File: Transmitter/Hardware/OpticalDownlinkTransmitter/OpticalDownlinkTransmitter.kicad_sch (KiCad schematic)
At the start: 34 parts, among them J1 Conn_01x04_Pin, J2 Conn_01x04_Pin, U1 AL8860MP, U2 AL8860MP, U3 AL8860MP, U4 AL8860MP

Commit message: Assigned a couple footprints
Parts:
- D11, D12, D13, D14, D15, D16, D7, D8: footprint (none) -> Footprint Library:OD624L
- D3, D4, D5, D6: footprint SamacSys_Parts:OD624L -> Footprint Library:OD624L
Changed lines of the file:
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@@
 			)
 		)
-		(property "Footprint" ""
+		(property "Footprint" "Footprint Library:OD624L"
 			(at 252.73 57.15 0)
 			(effects
@@
 			)
 		)
-		(property "Footprint" "SamacSys_Parts:OD624L"
+		(property "Footprint" "Footprint Library:OD624L"
 			(at 149.86 67.31 0)
 			(effects
@@
 			)
 		)
-		(property "Footprint" ""
+		(property "Footprint" "Footprint Library:OD624L"
 			(at 149.86 133.35 0)
 			(effects
@@
 			)
 		)
-		(property "Footprint" ""
+		(property "Footprint" "Footprint Library:OD624L"
 			(at 252.73 143.51 0)
 			(effects
@@
 			)
 		)
-		(property "Footprint" ""
+		(property "Footprint" "Footprint Library:OD624L"
 			(at 252.73 67.31 0)
 			(effects
@@
 			)
 		)
-		(property "Footprint" "SamacSys_Parts:OD624L"
+		(property "Footprint" "Footprint Library:OD624L"
 			(at 144.78 52.07 0)
 			(effects
@@
 			)
 		)
-		(property "Footprint" ""
+		(property "Footprint" "Footprint Library:OD624L"
 			(at 247.65 128.27 0)
 			(effects
@@
 			)
 		)
-		(property "Footprint" ""
+		(property "Footprint" "Footprint Library:OD624L"
 			(at 149.86 143.51 0)
 			(effects
@@
 			)
 		)
-		(property "Footprint" "SamacSys_Parts:OD624L"
+		(property "Footprint" "Footprint Library:OD624L"
 			(at 144.78 128.27 0)
 			(effects
@@
 			)
 		)
-		(property "Footprint" ""
+		(property "Footprint" "Footprint Library:OD624L"
 			(at 247.65 52.07 0)
 			(effects
@@
 			)
 		)
-		(property "Footprint" ""
+		(property "Footprint" "Footprint Library:OD624L"
 			(at 252.73 133.35 0)
 			(effects
@@
 			)
 		)
-		(property "Footprint" "SamacSys_Parts:OD624L"
+		(property "Footprint" "Footprint Library:OD624L"
 			(at 149.86 57.15 0)
 			(effects

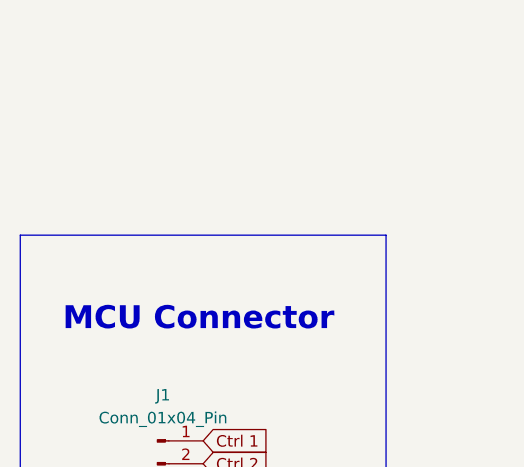
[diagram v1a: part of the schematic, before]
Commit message: Assigned a couple footprints and started adding JLBPCB Parts
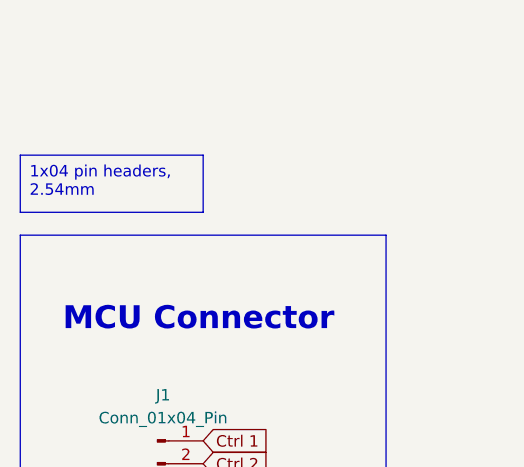
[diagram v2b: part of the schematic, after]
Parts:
- D3, D5, D6: JLCPCB Part (none) -> C20010764
- R1: footprint (none) -> Resistor_SMD:R_0805_2012Metric_Pad1.20x1.40mm_HandSolder; JLBPCB Part (none) -> C20485079
- R2: footprint (none) -> Resistor_SMD:R_0805_2012Metric_Pad1.20x1.40mm_HandSolder; Digikey Part (none) -> RLC73K2AR287FTD; JLCPCB Part (none) -> C20485079
- R3, R4: footprint (none) -> Resistor_SMD:R_0805_2012Metric_Pad1.20x1.40mm_HandSolder; JLCPCB Part (none) -> C20485079
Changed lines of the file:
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@@
 		)
 	)
+	(text_box "1x04 pin headers, 2.54mm\n"
+		(exclude_from_sim no)
+		(at 22.86 41.91 0)
+		(size 20.32 6.35)
+		(stroke
+			(width 0)
+			(type default)
+		)
+		(fill
+			(type none)
+		)
+		(effects
+			(font
+				(size 1.27 1.27)
+			)
+			(justify left top)
+		)
+	)
 	(text_box "I_{f} of each LED = 350mA\n\nR = 0.1/i_{out_nom} = 0.1/0.35A = 0.285  (p.11)"
 		(exclude_from_sim no)
@@
 			)
 		)
-		(property "Footprint" ""
+		(property "Footprint" "Resistor_SMD:R_0805_2012Metric_Pad1.20x1.40mm_HandSolder"
 			(at 236.22 126.492 90)
 			(effects
@@
 			)
 		)
+		(property "JLCPCB Part" "C20485079"
+			(at 236.22 128.27 90)
+			(effects
+				(font
+					(size 1.27 1.27)
+				)
+				(hide yes)
+			)
+		)
 		(pin "2"
 		)
@@
 			)
 		)
-		(property "Footprint" ""
+		(property "Footprint" "Resistor_SMD:R_0805_2012Metric_Pad1.20x1.40mm_HandSolder"
 			(at 133.35 50.292 90)
 			(effects
@@
 			)
 		)
+		(property "JLBPCB Part" "C20485079"
+			(at 133.35 52.07 90)
+			(effects
+				(font
+					(size 1.27 1.27)
+				)
+				(hide yes)
+			)
+		)
 		(pin "2"
 		)
@@
 			)
 		)
+		(property "JLCPCB Part" "C20010764"
+			(at 149.86 67.31 0)
+			(effects
+				(font
+					(size 1.27 1.27)
+				)
+				(hide yes)
+			)
+		)
 		(pin "1"
 		)
@@
 			)
 		)
+		(property "JLCPCB Part" "C20010764"
+			(at 144.78 52.07 0)
+			(effects
+				(font
+					(size 1.27 1.27)
+				)
+				(hide yes)
+			)
+		)
 		(pin "2"
 		)
@@
 			)
 		)
-		(property "Footprint" ""
+		(property "Footprint" "Resistor_SMD:R_0805_2012Metric_Pad1.20x1.40mm_HandSolder"
 			(at 236.22 50.292 90)
 			(effects
@@
 			)
 		)
+		(property "JLCPCB Part" "C20485079"
+			(at 236.22 52.07 90)
+			(effects
+				(font
+					(size 1.27 1.27)
+				)
+				(hide yes)
+			)
+		)
 		(pin "2"
 		)
@@
 			)
 		)
-		(property "Footprint" ""
+		(property "Footprint" "Resistor_SMD:R_0805_2012Metric_Pad1.20x1.40mm_HandSolder"
 			(at 133.35 126.492 90)
 			(effects
@@
 			)
 		)
+		(property "Digikey Part" "RLC73K2AR287FTD"
+			(at 133.35 128.27 90)
+			(effects
+				(font
+					(size 1.27 1.27)
+				)
+				(hide yes)
+			)
+		)
+		(property "JLCPCB Part" "C20485079"
+			(at 133.35 128.27 90)
+			(effects
+				(font
+					(size 1.27 1.27)
+				)
+				(hide yes)
+			)
+		)
 		(pin "2"
 		)
@@
 			(at 149.86 57.15 0)
 			(effects
+				(font
+					(size 1.27 1.27)
+				)
+				(hide yes)
+			)
+		)
+		(property "JLCPCB Part" "C20010764"
+			(at 149.86 57.15 0)
+			(effects

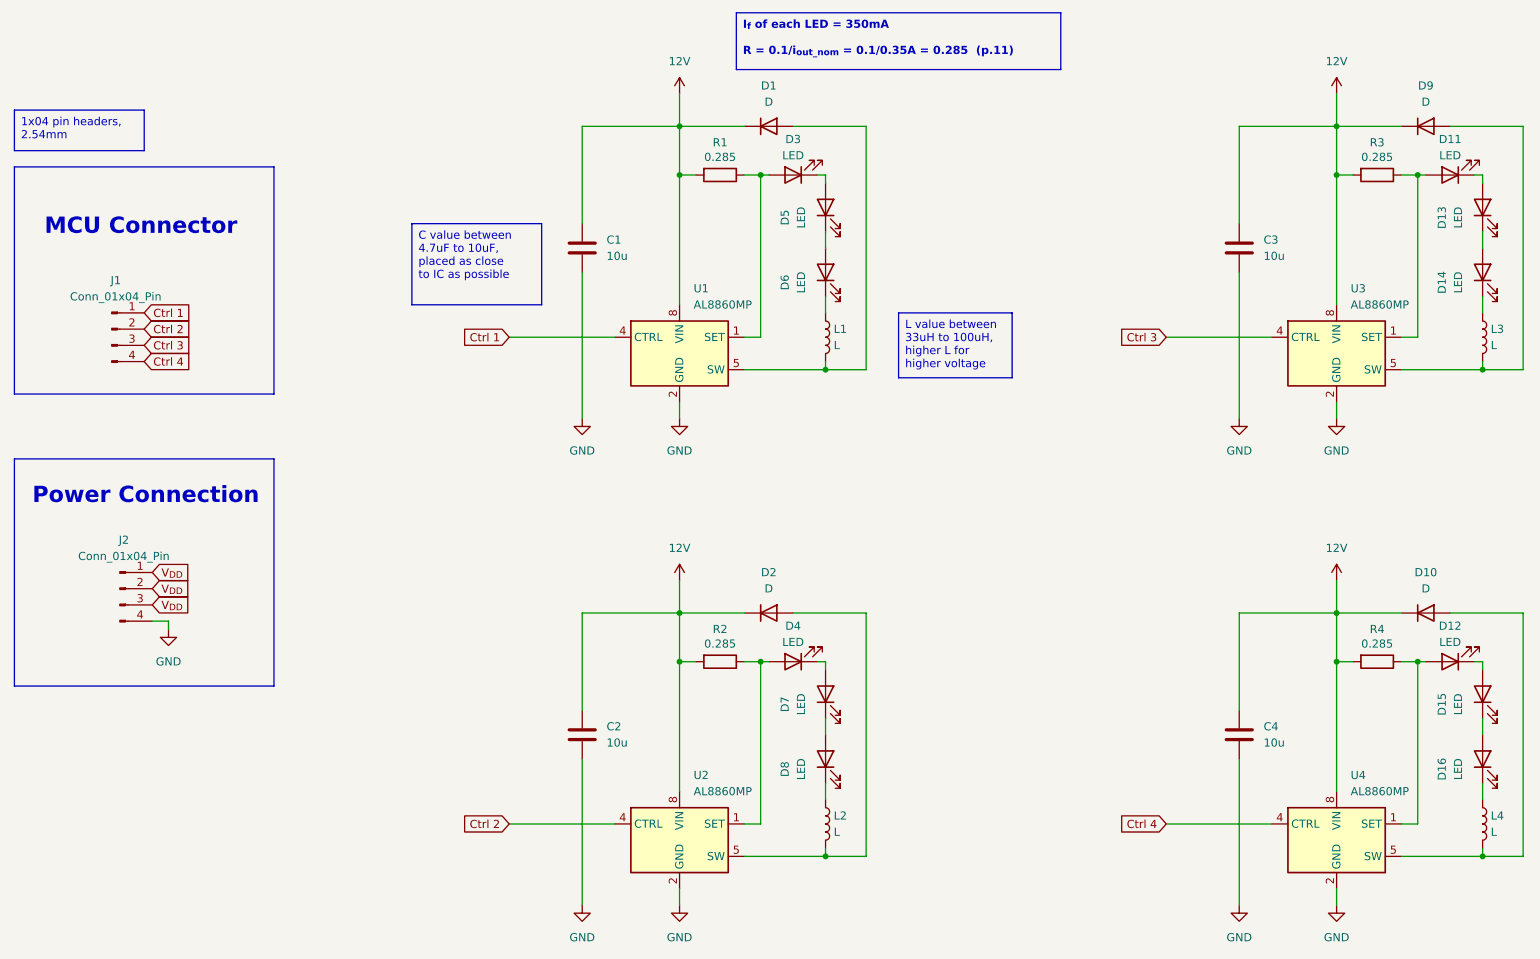
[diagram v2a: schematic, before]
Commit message: Assigned JLCPCB Parts and footprints
Inductor is the remaining component left to find
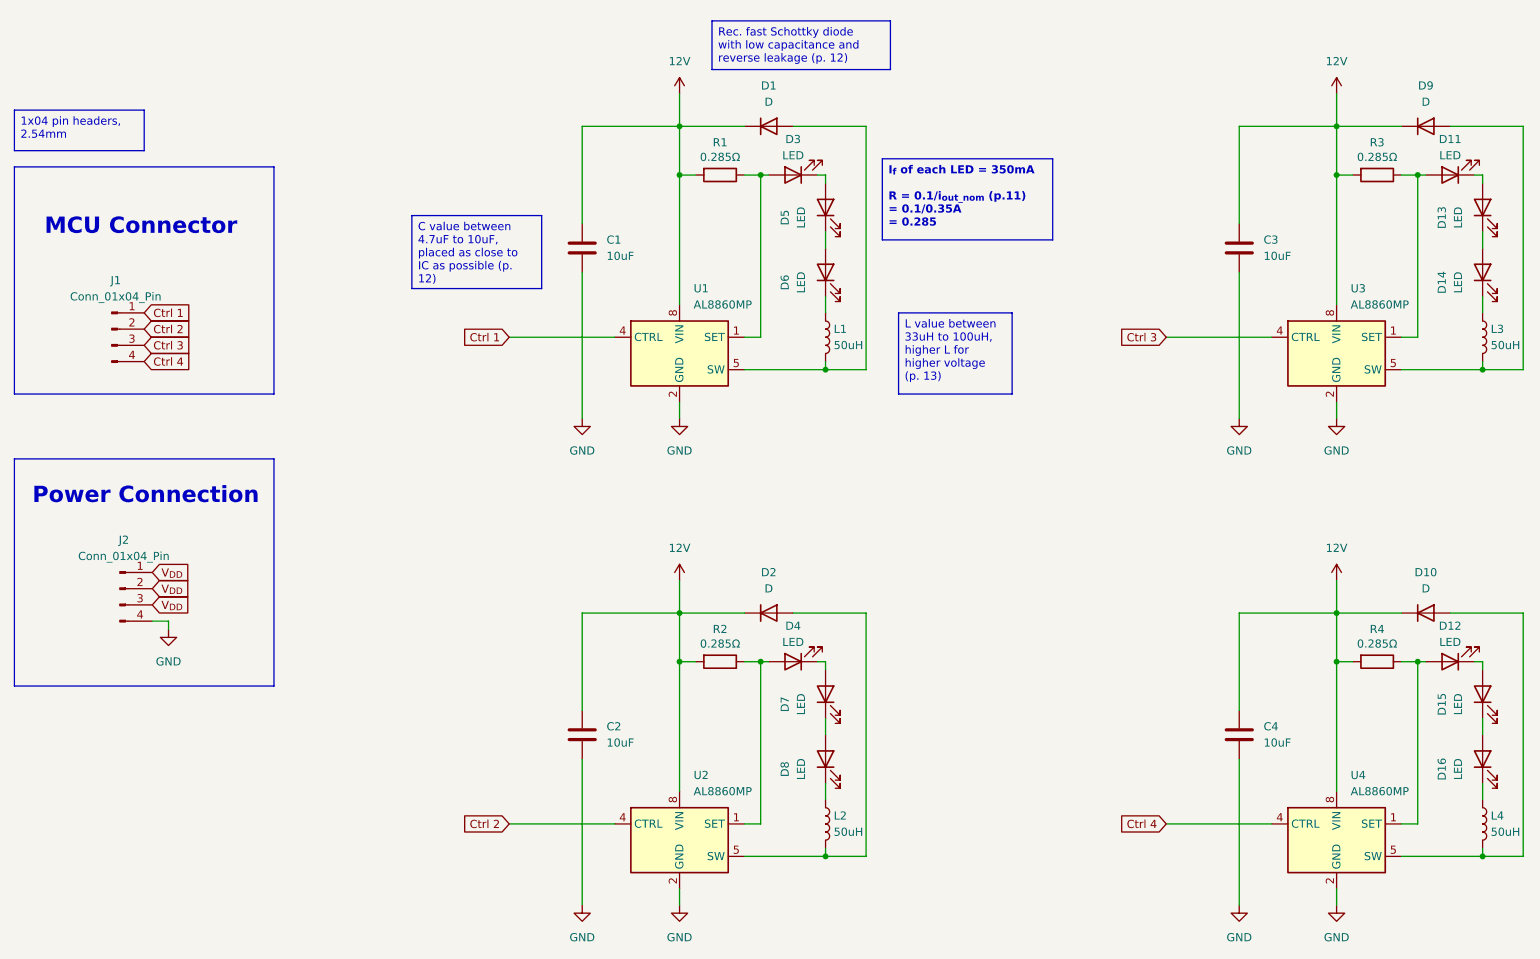
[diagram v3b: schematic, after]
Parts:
- C1, C2, C3, C4: value 10u -> 10uF
- D1, D10, D2, D9: footprint (none) -> Footprint Library:P2_DO-201; JLCPCB Part (none) -> C5357977
- D11, D12, D13, D14, D15, D16, D4, D7, D8: JLCPCB Part (none) -> C20010764
- J1, J2: footprint (none) -> Connector_PinSocket_2.54mm:PinSocket_1x04_P2.54mm_Vertical
- L1, L2, L3, L4: value L -> 50uH
- R1, R2, R3, R4: value 0.285 -> 0.285Ω
- U1, U2, U3, U4: JLCPCB Part (none) -> C500782

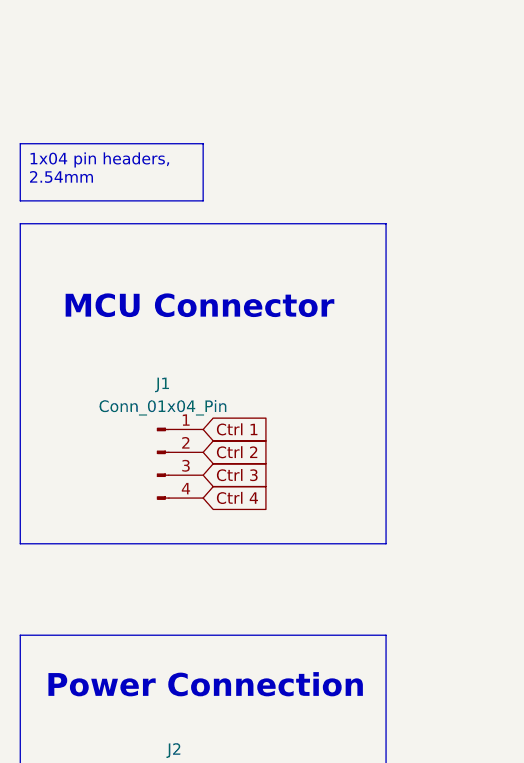
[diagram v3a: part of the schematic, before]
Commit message: Assigned JLCPCB Parts
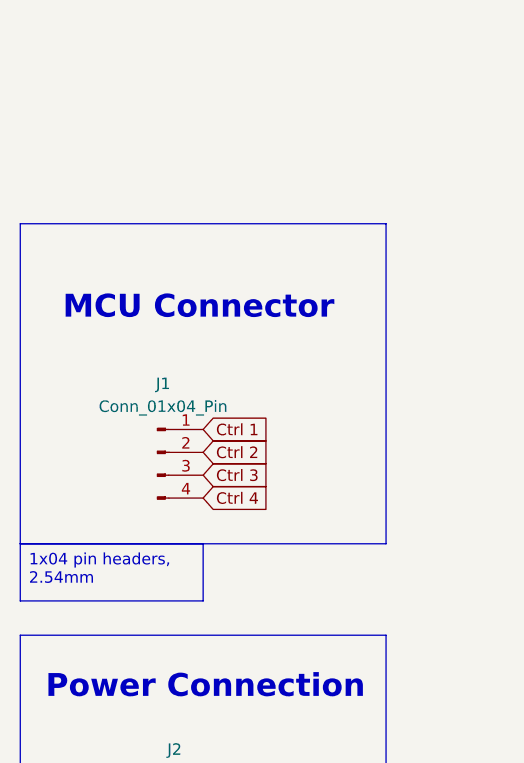
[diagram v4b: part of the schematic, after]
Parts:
- C1, C2, C3, C4: footprint (none) -> Capacitor_SMD:C_0805_2012Metric_Pad1.18x1.45mm_HandSolder; JLCPCB Part (none) -> C95841
- L1, L2, L3, L4: footprint (none) -> Footprint Library:DR125; JLCPCB Part (none) -> C5120951
- R1: JLBPCB Part C20485079 -> (none); JLCPCB Part (none) -> C20485079
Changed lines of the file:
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@@
 	(text_box "1x04 pin headers, 2.54mm\n"
 		(exclude_from_sim no)
-		(at 22.86 41.91 0)
+		(at 22.86 86.36 0)
 		(size 20.32 6.35)
 		(margins 0.9525 0.9525 0.9525 0.9525)
@@
 			)
 		)
-		(property "Footprint" ""
+		(property "Footprint" "Footprint Library:DR125"
 			(at 252.73 77.47 0)
 			(effects
@@
 			)
 		)
+		(property "JLCPCB Part" "C5120951"
+			(at 252.73 77.47 0)
+			(effects
+				(font
+					(size 1.27 1.27)
+				)
+				(hide yes)
+			)
+		)
 		(pin "1"
 		)
@@
 			)
 		)
-		(property "Footprint" ""
+		(property "Footprint" "Footprint Library:DR125"
 			(at 149.86 77.47 0)
 			(effects
@@
 			)
 		)
+		(property "JLCPCB Part" "C5120951"
+			(at 149.86 77.47 0)
+			(effects
+				(font
+					(size 1.27 1.27)
+				)
+				(hide yes)
+			)
+		)
 		(pin "1"
 		)
@@
 			)
 		)
-		(property "JLBPCB Part" "C20485079"
+		(property "JLCPCB Part" "C20485079"
 			(at 133.35 52.07 90)
 			(effects
@@
 			)
 		)
-		(property "Footprint" ""
+		(property "Footprint" "Capacitor_SMD:C_0805_2012Metric_Pad1.18x1.45mm_HandSolder"
 			(at 112.7252 67.31 0)
 			(effects
@@
 			)
 		)
+		(property "JLCPCB Part" "C95841"
+			(at 111.76 63.5 0)
+			(effects
+				(font
+					(size 1.27 1.27)
+				)
+				(hide yes)
+			)
+		)
 		(pin "1"
 		)
@@
 			)
 		)
-		(property "Footprint" ""
+		(property "Footprint" "Footprint Library:DR125"
 			(at 252.73 153.67 0)
 			(effects
@@
 			)
 		)
+		(property "JLCPCB Part" "C5120951"
+			(at 252.73 153.67 0)
+			(effects
+				(font
+					(size 1.27 1.27)
+				)
+				(hide yes)
+			)
+		)
 		(pin "1"
 		)
@@
 			)
 		)
-		(property "Footprint" ""
+		(property "Footprint" "Capacitor_SMD:C_0805_2012Metric_Pad1.18x1.45mm_HandSolder"
 			(at 215.5952 143.51 0)
 			(effects
@@
 			)
 		)
+		(property "JLCPCB Part" "C95841"
+			(at 214.63 139.7 0)
+			(effects
+				(font
+					(size 1.27 1.27)
+				)
+				(hide yes)
+			)
+		)
 		(pin "1"
 		)
@@
 			)
 		)
-		(property "Footprint" ""
+		(property "Footprint" "Capacitor_SMD:C_0805_2012Metric_Pad1.18x1.45mm_HandSolder"
 			(at 112.7252 143.51 0)
 			(effects
@@
 			)
 		)
+		(property "JLCPCB Part" "C95841"
+			(at 111.76 139.7 0)
+			(effects
+				(font
+					(size 1.27 1.27)
+				)
+				(hide yes)
+			)
+		)
 		(pin "1"
 		)
@@
 			)
 		)
-		(property "Footprint" ""
+		(property "Footprint" "Capacitor_SMD:C_0805_2012Metric_Pad1.18x1.45mm_HandSolder"
 			(at 215.5952 67.31 0)
 			(effects
@@
 			)
 		)
+		(property "JLCPCB Part" "C95841"
+			(at 214.63 63.5 0)
+			(effects
+				(font
+					(size 1.27 1.27)
+				)
+				(hide yes)
+			)
+		)
 		(pin "1"
 		)
@@
 			)
 		)
-		(property "Footprint" ""
+		(property "Footprint" "Footprint Library:DR125"
 			(at 149.86 153.67 0)
 			(effects
@@
 			(at 149.86 153.67 0)
 			(effects
+				(font
+					(size 1.27 1.27)
+				)
+				(hide yes)
+			)
+		)
+		(property "JLCPCB Part" "C5120951"
+			(at 149.86 153.67 0)
+			(effects
